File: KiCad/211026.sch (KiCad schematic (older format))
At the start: 0 parts

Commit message: update schematics and libraries
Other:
- note added: "Non-inverseur avec\nalimentation unipolaire\n"
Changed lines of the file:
@@
 F1 "C.sch" 50
 $EndSheet
+Text Notes 850  1350 0    50   ~ 0
+Non-inverseur avec\nalimentation unipolaire\n
 $EndSCHEMATC

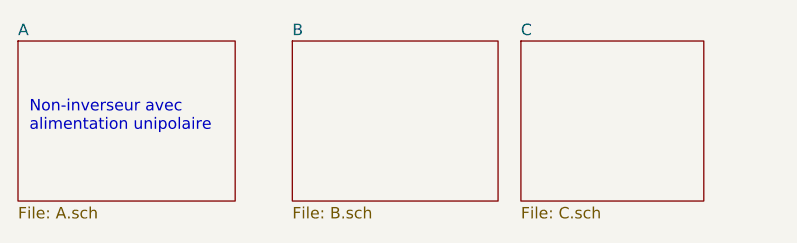
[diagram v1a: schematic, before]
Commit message: corrected opamp circuits
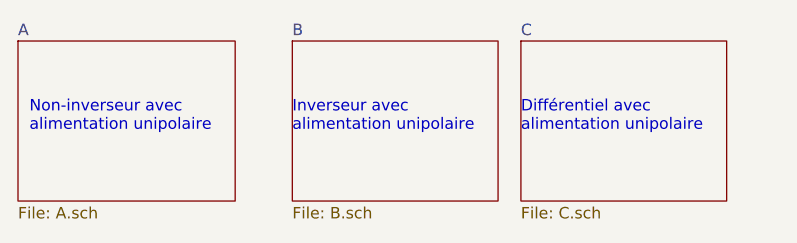
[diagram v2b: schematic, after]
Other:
- note added: "Différentiel avec\nalimentation unipolaire\n"
- note added: "Inverseur avec\nalimentation unipolaire\n"
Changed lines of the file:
@@
 $EndSheet
 $Sheet
-S 3000 950  800  700
+S 3000 950  900  700
 U 6178A189
 F0 "C" 50
@@
 Text Notes 850  1350 0    50   ~ 0
 Non-inverseur avec\nalimentation unipolaire\n
+Text Notes 2000 1350 0    50   ~ 0
+Inverseur avec\nalimentation unipolaire\n
+Text Notes 3000 1350 0    50   ~ 0
+Différentiel avec\nalimentation unipolaire\n
 $EndSCHEMATC
